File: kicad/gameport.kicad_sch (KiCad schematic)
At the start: 0 parts

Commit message: update kicad project
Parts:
- added J6: Gameport Header, seequa_footprints:PinHeader_Gameport_Vertical, symbol seequa:Gameport Header
- added U120: 74LS244, Package_DIP:DIP-20_W7.62mm_Socket, symbol 74xx:74LS244
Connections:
- new net +5V: J6.1 (+5V), J6.8 (+5V), J6.9 (+5V)
- new net PD0: U120.3 (O3b)

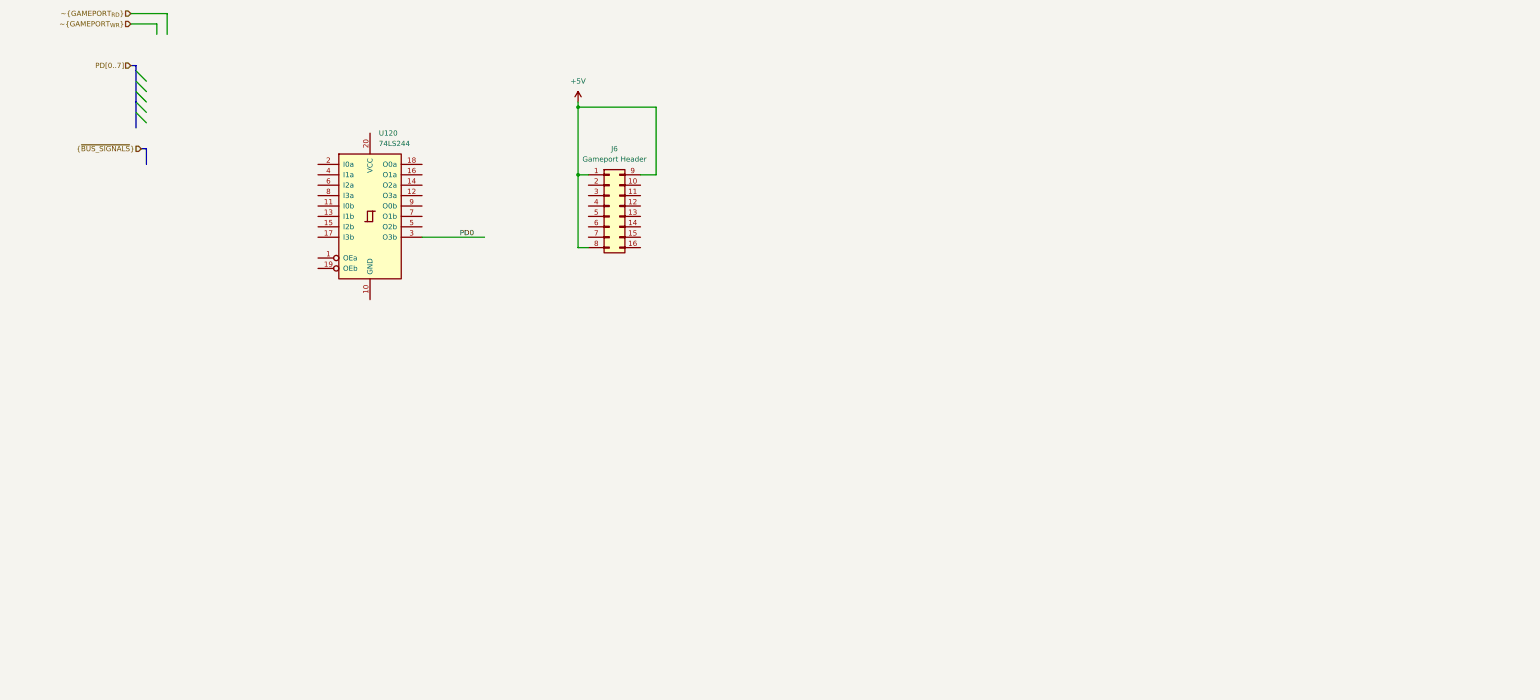
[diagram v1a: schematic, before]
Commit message: Add parallel port, game port
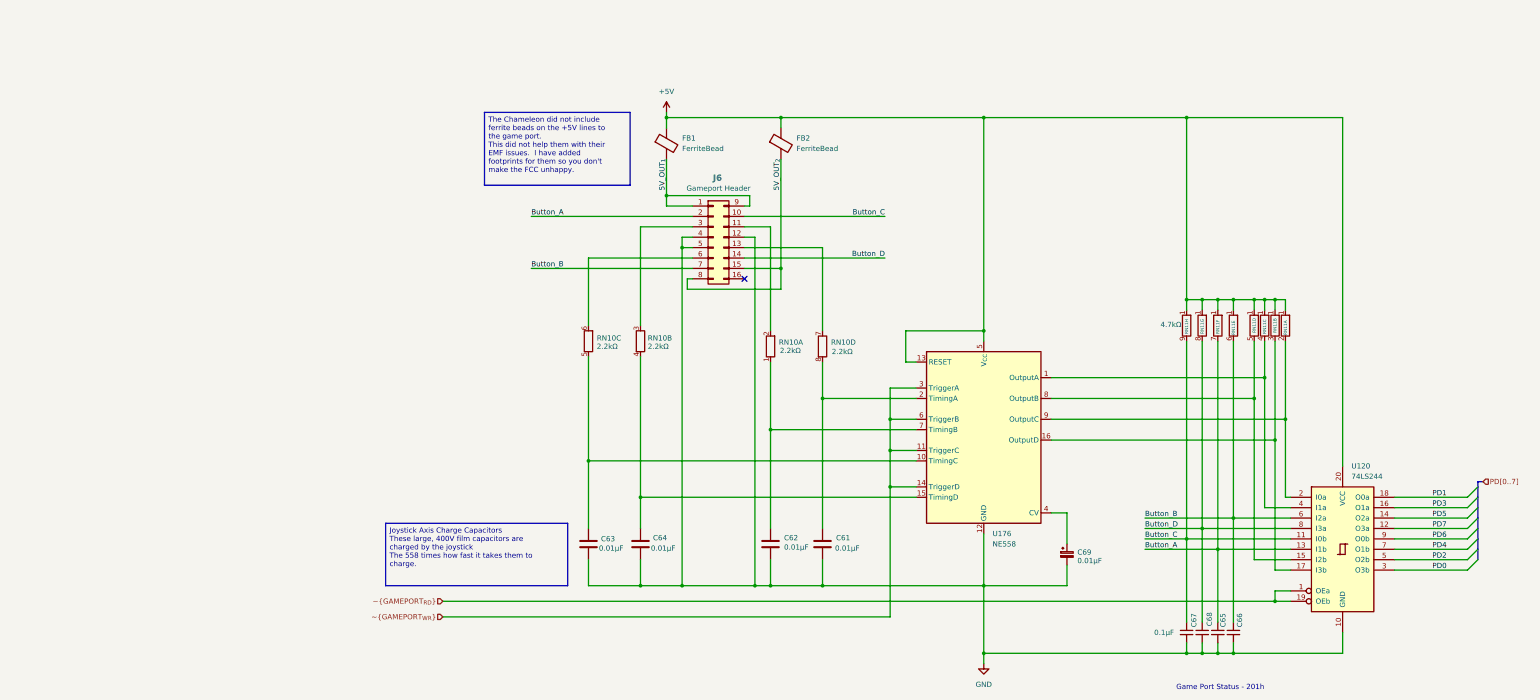
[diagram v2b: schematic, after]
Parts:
- added C61, C62, C63, C64: 0.01µF, Capacitor_THT:C_Rect_L11.5mm_W2.0mm_P10.00mm_MKT, symbol Device:C
- added C65, C66, C68: C_Small, seequa_footprints:C_Seequa_Clock_Cap_6.35mm, symbol Device:C_Small
- added C67: 0.1µF, seequa_footprints:C_Seequa_Clock_Cap_6.35mm, symbol Device:C_Small
- added C69: 0.01µF, seequa_footprints:C_Seequa_Bypass_3.8mm, symbol seequa:C_Bypass_3.8mm
- added FB1, FB2: FerriteBead, Inductor_THT:L_Axial_L5.3mm_D2.2mm_P7.62mm_Horizontal_Vishay_IM-1, symbol Device:FerriteBead
- added RN10: 2.2kΩ, Resistor_THT:R_Array_SIP8, symbol Device:R_Pack04_SIP_Split
- added RN11: 4.7kΩ, Resistor_THT:R_Array_SIP10, symbol Device:R_Network09_Split
- added U176: NE558, Package_DIP:DIP-16_W7.62mm, symbol seequa:NE558
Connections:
- net +5V: now also U120.20 (VCC), FB1.1, FB2.1, RN11.1 (R1), RN11.1 (R1), RN11.1 (R1), RN11.1 (R1), RN11.1 (R1), RN11.1 (R1), RN11.1 (R1), RN11.1 (R1), U176.13 (RESET), U176.5 (V_{CC}); no longer J6.1 (+5V), J6.8 (+5V), J6.9 (+5V)
- net ~{GAMEPORT_{RD}}: now also U120.1 (OEa), U120.19 (OEb)
- net ~{GAMEPORT_{WR}}: now also U176.11 (TriggerC), U176.14 (TriggerD), U176.3 (TriggerA), U176.6 (TriggerB)
- net GND: now reaches U120.10 (GND)
- net GND: now also J6.12 (GND), J6.4 (GND), J6.5 (GND), C61.2, C62.2, C63.2, C64.2, C65.2, C66.2, C67.2, C68.2, C69.2, U176.12 (GND)
- net Button_C: now reaches U120.11 (I0b)
- net Button_C: now also J6.10 (Button_C), C67.1, RN11.9 (R8.2)
- net PD7: now reaches U120.12 (O3a)
- net Button_A: now reaches U120.13 (I1b)
- net Button_A: now also J6.2 (Button_A), C65.1, RN11.7 (R6.2)
- net PD5: now reaches U120.14 (O2a)
- net at U120.15 (I2b): now also RN11.5 (R4.2), U176.8 (OutputB)
- net PD3: now reaches U120.16 (O1a)
- net at U120.17 (I3b): now also RN11.3 (R2.2), U176.16 (OutputD)
- net PD1: now reaches U120.18 (O0a)
- net at U120.2 (I0a): now also RN11.2 (R1.2), U176.9 (OutputC)
- net at U120.4 (I1a): now also RN11.4 (R3.2), U176.1 (OutputA)
- net PD2: now reaches U120.5 (O2b)
- net Button_B: now reaches U120.6 (I2a)
- net Button_B: now also J6.7 (Button_B), C66.1, RN11.6 (R5.2)
- net PD4: now reaches U120.7 (O1b)
- net Button_D: now reaches U120.8 (I3a)
- net Button_D: now also J6.14 (Button_D), C68.1, RN11.8 (R7.2)
- net PD6: now reaches U120.9 (O0b)
- net at J6.11 (Position_C): now also RN10.2 (R1.2)
- net at J6.13 (Position_D): now also RN10.7 (R4.1)
- net 5V_OUT_{2}: now reaches J6.15 (+5V)
- net 5V_OUT_{2}: now also J6.8 (+5V), FB2.2
- net at J6.3 (Position_A): now also RN10.3 (R2.1)
- net at J6.6 (Position_B): now also RN10.6 (R3.2)
- new net: C62.1, RN10.1 (R1.1), U176.7 (TimingB)
- new net: C61.1, RN10.8 (R4.2), U176.2 (TimingA)
- new net: C63.1, RN10.5 (R3.1), U176.10 (TimingC)
- new net: C69.1, U176.4 (CV)
- new net: C64.1, RN10.4 (R2.2), U176.15 (TimingD)
- new net 5V_OUT_{1}: FB1.2, J6.1 (+5V), J6.9 (+5V)
- no-connect marks 0 -> 1
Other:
- note added: "Game Port Status - 201h"
- title: (none) -> Game Port
- moved on the sheet: J6, U120
